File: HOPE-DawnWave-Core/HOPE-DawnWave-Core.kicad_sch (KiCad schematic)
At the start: 40 parts, among them J1 USB_C_Receptacle_USB2.0_16P, SW1 RST, SW2 BOOT, U1 TLV62569DRL, U2 USBLC6-2P6, U3 ESP32-C6-WROOM-1

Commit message: positions of some components - buck converter and usb c - completed
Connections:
- net D+: now also U2.6 (I/O1); no longer U2.4 (I/O2)
- net D-: now also U2.4 (I/O2); no longer U2.6 (I/O1)
- net USB_D+: now also U2.1 (I/O1); no longer U2.3 (I/O2)
- net USB_D-: now also U2.3 (I/O2); no longer U2.1 (I/O1)
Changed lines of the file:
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@@
 		)
 	)
-	(label "D-"
+	(label "D+"
 		(at 81.28 55.88 180)
 		(fields_autoplaced yes)
@@
 		)
 	)
-	(label "USB_D-"
+	(label "USB_D+"
 		(at 57.15 55.88 0)
 		(fields_autoplaced yes)
@@
 		)
 	)
-	(label "D+"
+	(label "D-"
 		(at 81.28 58.42 180)
 		(fields_autoplaced yes)
@@
 		)
 	)
-	(label "USB_D+"
+	(label "USB_D-"
 		(at 57.15 58.42 0)
 		(fields_autoplaced yes)

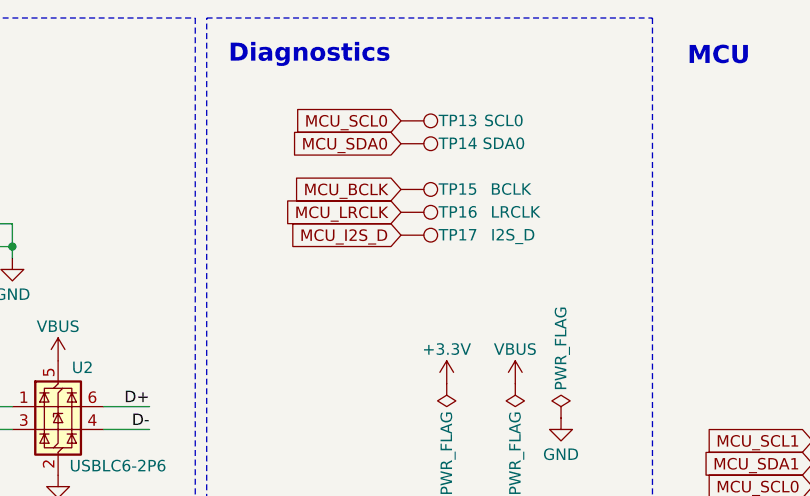
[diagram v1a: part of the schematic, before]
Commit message: flipped esp32 to keep 3.3v on right and 5v on left
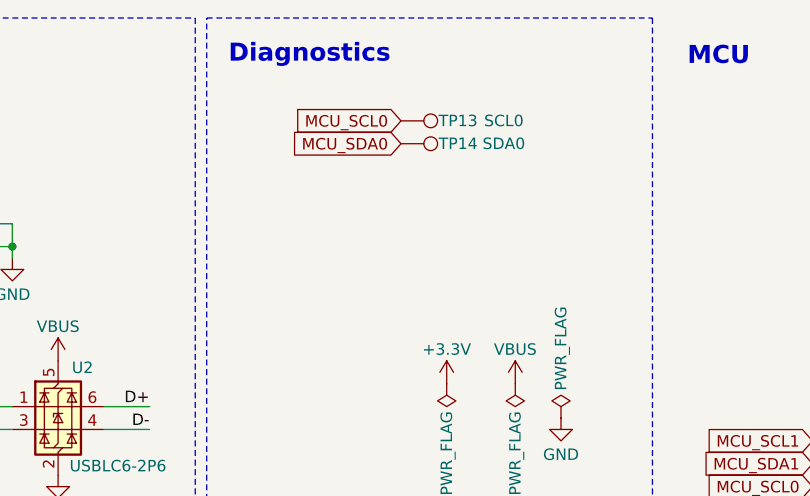
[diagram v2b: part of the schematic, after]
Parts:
- removed TP15: BCLK, TestPoint:TestPoint_Pad_D1.5mm, symbol Connector:TestPoint
- removed TP16: LRCLK, TestPoint:TestPoint_Pad_D1.5mm, symbol Connector:TestPoint
- removed TP17: I2S_D, TestPoint:TestPoint_Pad_D1.5mm, symbol Connector:TestPoint
- TP13, TP14: footprint TestPoint:TestPoint_Pad_D1.5mm -> TestPoint:TestPoint_Pad_D1.0mm

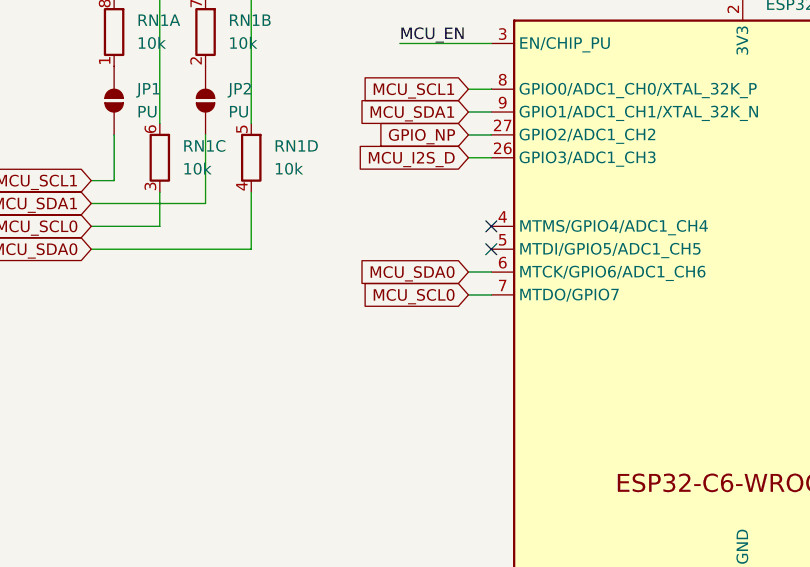
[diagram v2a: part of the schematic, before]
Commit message: fixed gitignore and completed major component placement iteration
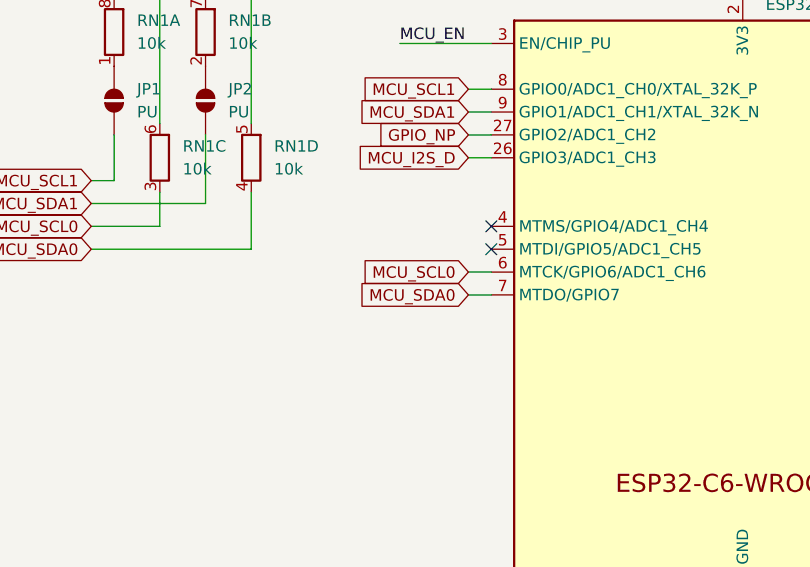
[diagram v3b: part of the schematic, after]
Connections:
- net MCU_SCL0: now also U3.6 (MTCK/GPIO6/ADC1_CH6); no longer U3.7 (MTDO/GPIO7)
- net MCU_SDA0: now also U3.7 (MTDO/GPIO7); no longer U3.6 (MTCK/GPIO6/ADC1_CH6)

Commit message: big progress oops
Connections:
- net GPIO_NP: now also U3.19 (GPIO21); no longer U3.27 (GPIO2/ADC1_CH2)
- net MCU_BACKLIGHT: now also U3.12 (GPIO11); no longer U3.23 (GPIO15)
- net MCU_BCLK: now also U3.17 (GPIO19); no longer U3.25 (U0TXD/GPIO16)
- net MCU_DRST: now also U3.23 (GPIO15); no longer U3.11 (GPIO10)
- net MCU_D/C: now also U3.27 (GPIO2/ADC1_CH2); no longer U3.19 (GPIO21)
- net MCU_I2S_D: now also U3.18 (GPIO20); no longer U3.26 (GPIO3/ADC1_CH3)
- net MCU_LRCLK: now also U3.16 (GPIO18); no longer U3.24 (U0RXD/GPIO17)
- net MCU_MISO: now also U3.24 (U0RXD/GPIO17); no longer U3.16 (GPIO18)
- net MCU_MOSI: now also U3.26 (GPIO3/ADC1_CH3); no longer U3.18 (GPIO20)
- net MCU_SCL0: now also U3.7 (MTDO/GPIO7); no longer U3.6 (MTCK/GPIO6/ADC1_CH6)
- net MCU_SCLK: now also U3.25 (U0TXD/GPIO16); no longer U3.17 (GPIO19)
- net MCU_SDA0: now also U3.6 (MTCK/GPIO6/ADC1_CH6); no longer U3.7 (MTDO/GPIO7)
- net MCU_TD: now also U3.11 (GPIO10); no longer U3.12 (GPIO11)

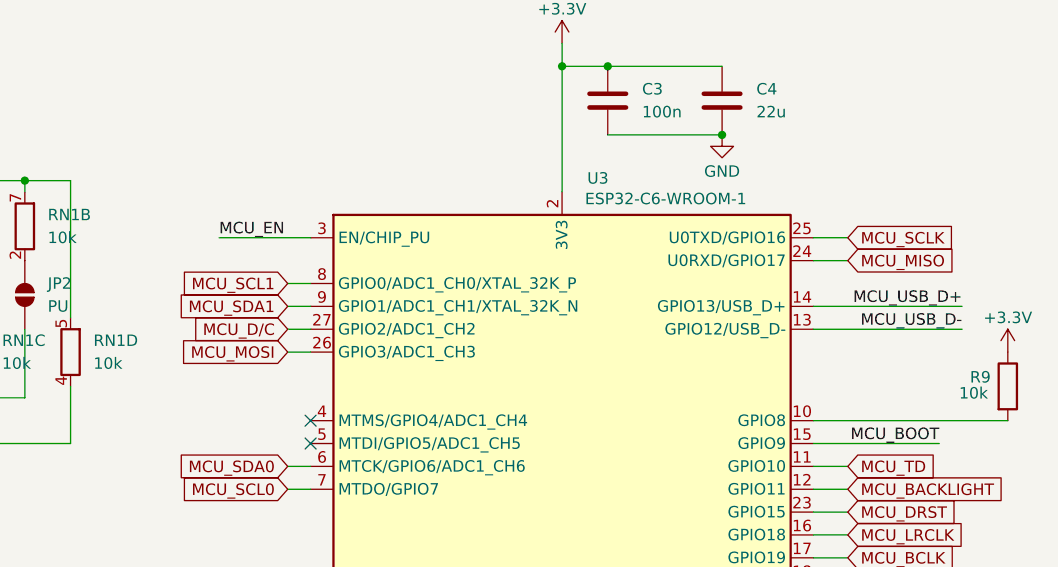
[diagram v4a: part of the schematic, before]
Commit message: Initial layout, need to resolve errors
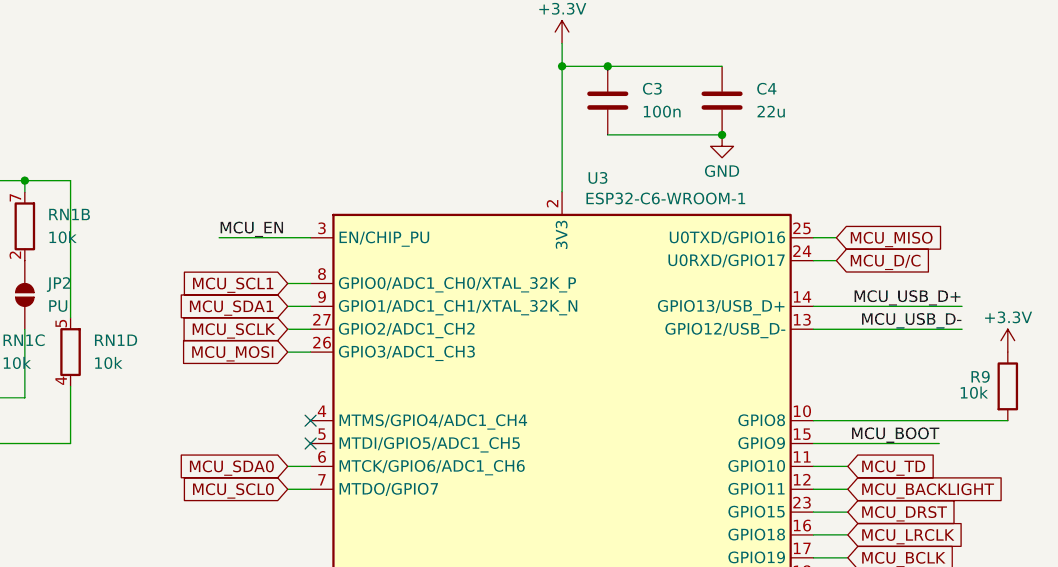
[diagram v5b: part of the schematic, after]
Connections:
- net MCU_D/C: now also U3.24 (U0RXD/GPIO17); no longer U3.27 (GPIO2/ADC1_CH2)
- net MCU_MISO: now also U3.25 (U0TXD/GPIO16); no longer U3.24 (U0RXD/GPIO17)
- net MCU_SCLK: now also U3.27 (GPIO2/ADC1_CH2); no longer U3.25 (U0TXD/GPIO16)

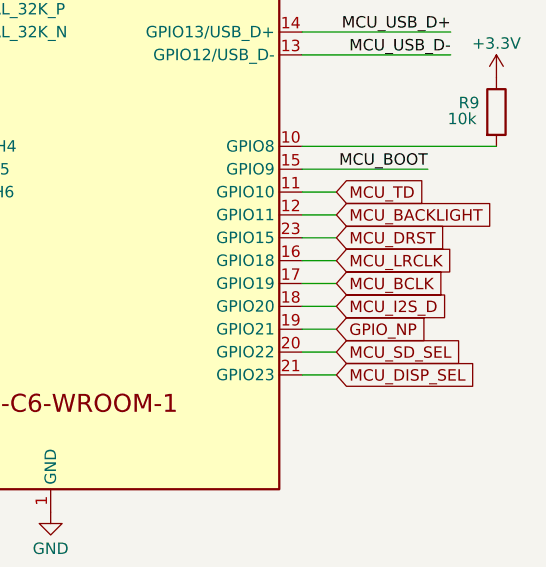
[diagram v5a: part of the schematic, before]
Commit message: fixed spacing on high speed lines, added ground via stitching, made power polygons a bit cleaner, silkscreen labeling is still not done but all warnings are gone
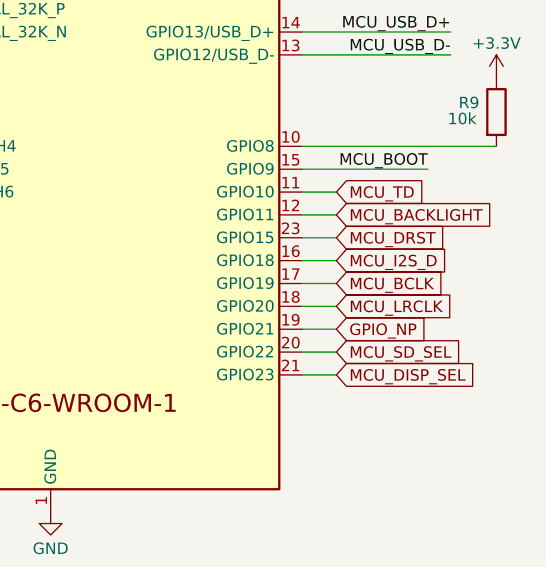
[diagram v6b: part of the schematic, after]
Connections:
- net MCU_I2S_D: now also U3.16 (GPIO18); no longer U3.18 (GPIO20)
- net MCU_LRCLK: now also U3.18 (GPIO20); no longer U3.16 (GPIO18)

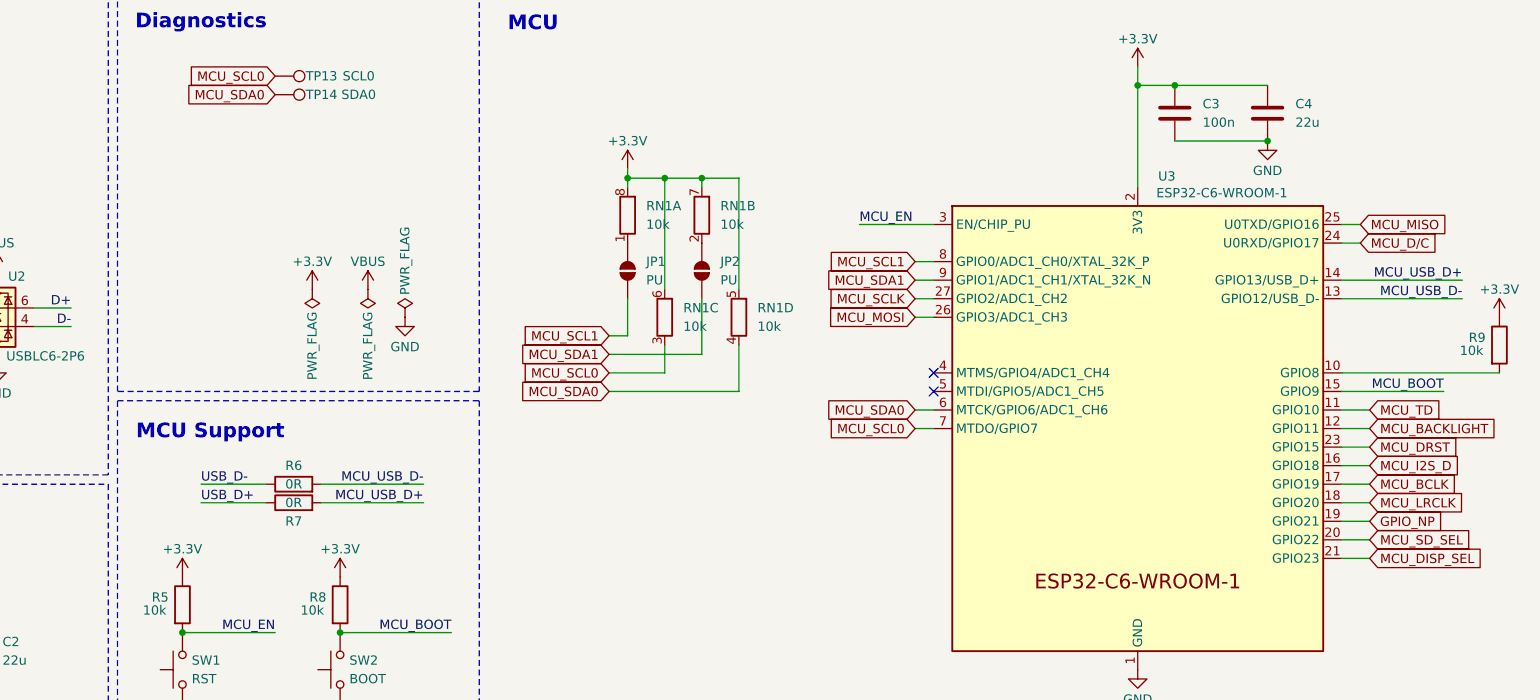
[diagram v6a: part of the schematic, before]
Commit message: corrected eyespi connector wiring and added a 2.54mm pitch header to break it out in case something bad happens
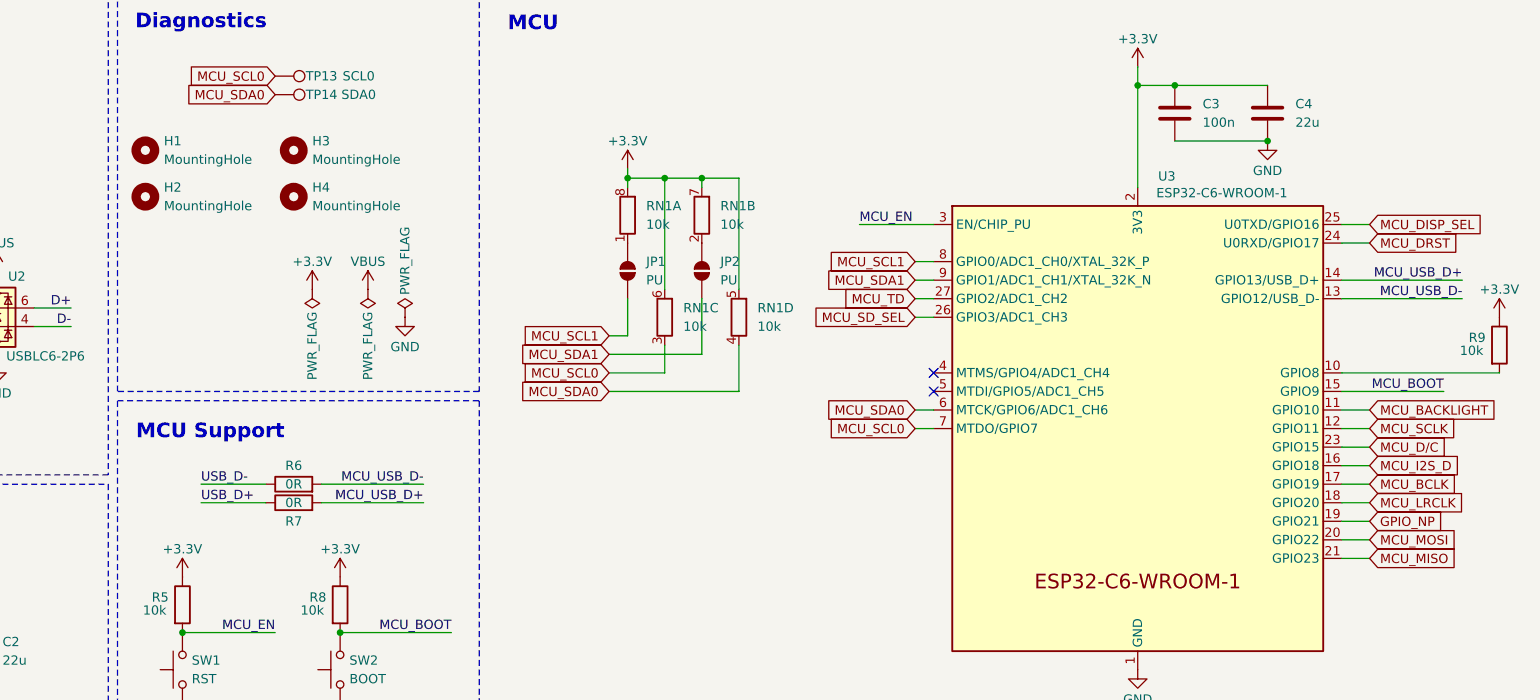
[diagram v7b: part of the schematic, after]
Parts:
- added H1, H2, H3, H4: MountingHole, MountingHole:MountingHole_3.2mm_M3_ISO7380_Pad, symbol Mechanical:MountingHole
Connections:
- net MCU_BACKLIGHT: now also U3.11 (GPIO10); no longer U3.12 (GPIO11)
- net MCU_DISP_SEL: now also U3.25 (U0TXD/GPIO16); no longer U3.21 (GPIO23)
- net MCU_DRST: now also U3.24 (U0RXD/GPIO17); no longer U3.23 (GPIO15)
- net MCU_D/C: now also U3.23 (GPIO15); no longer U3.24 (U0RXD/GPIO17)
- net MCU_MISO: now also U3.21 (GPIO23); no longer U3.25 (U0TXD/GPIO16)
- net MCU_MOSI: now also U3.20 (GPIO22); no longer U3.26 (GPIO3/ADC1_CH3)
- net MCU_SCLK: now also U3.12 (GPIO11); no longer U3.27 (GPIO2/ADC1_CH2)
- net MCU_SD_SEL: now also U3.26 (GPIO3/ADC1_CH3); no longer U3.20 (GPIO22)
- net MCU_TD: now also U3.27 (GPIO2/ADC1_CH2); no longer U3.11 (GPIO10)

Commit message: fab files generated, pcb finalized
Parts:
- R6, R7: value 0R -> 27R
- RN1: value 10k -> 4.7k
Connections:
- net D+: now also U2.4 (I/O2); no longer U2.6 (I/O1)
- net D-: now also U2.6 (I/O1); no longer U2.4 (I/O2)
- net USB_D+: now also U2.3 (I/O2); no longer U2.1 (I/O1)
- net USB_D-: now also U2.1 (I/O1); no longer U2.3 (I/O2)
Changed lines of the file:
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@@
 	(wire
 		(pts
-			(xy 196.85 72.39) (xy 199.39 72.39)
-		)
-		(stroke
-			(width 0)
-			(type default)
-		)
-	)
-	(wire
-		(pts
 			(xy 26.67 68.58) (xy 34.29 68.58)
 		)
@@
 	(wire
 		(pts
+			(xy 196.85 72.39) (xy 199.39 72.39)
+		)
+		(stroke
+			(width 0)
+			(type default)
+		)
+	)
+	(wire
+		(pts
 			(xy 64.77 96.52) (xy 68.58 96.52)
 		)
@@
 	(wire
 		(pts
-			(xy 255.27 72.39) (xy 259.08 72.39)
+			(xy 196.85 69.85) (xy 199.39 69.85)
 		)
 		(stroke
@@
 	(wire
 		(pts
-			(xy 255.27 64.77) (xy 276.86 64.77)
+			(xy 255.27 72.39) (xy 259.08 72.39)
 		)
 		(stroke
@@
 	(wire
 		(pts
-			(xy 55.88 104.14) (xy 49.53 104.14)
+			(xy 255.27 64.77) (xy 276.86 64.77)
 		)
 		(stroke
@@
 	(wire
 		(pts
-			(xy 172.72 38.1) (xy 172.72 53.34)
+			(xy 55.88 104.14) (xy 49.53 104.14)
 		)
 		(stroke
@@
 	(wire
 		(pts
-			(xy 66.04 35.56) (xy 66.04 38.1)
+			(xy 172.72 38.1) (xy 172.72 53.34)
 		)
 		(stroke
@@
 	(wire
 		(pts
-			(xy 196.85 49.53) (xy 199.39 49.53)
+			(xy 66.04 35.56) (xy 66.04 38.1)
 		)
 		(stroke
@@
 	(wire
 		(pts
-			(xy 182.88 138.43) (xy 185.42 138.43)
+			(xy 196.85 49.53) (xy 199.39 49.53)
 		)
 		(stroke
@@
 	(wire
 		(pts
-			(xy 57.15 35.56) (xy 66.04 35.56)
+			(xy 182.88 138.43) (xy 185.42 138.43)
 		)
 		(stroke
@@
 	(wire
 		(pts
-			(xy 57.15 58.42) (xy 66.04 58.42)
+			(xy 76.2 58.42) (xy 81.28 58.42)
 		)
 		(stroke
@@
 	(wire
 		(pts
-			(xy 76.2 55.88) (xy 81.28 55.88)
+			(xy 57.15 35.56) (xy 66.04 35.56)
 		)
 		(stroke
@@
 	(wire
 		(pts
-			(xy 76.2 58.42) (xy 81.28 58.42)
-		)
-		(stroke
-			(width 0)
-			(type default)
-		)
-	)
-	(wire
-		(pts
-			(xy 196.85 69.85) (xy 199.39 69.85)
+			(xy 76.2 55.88) (xy 81.28 55.88)
 		)
 		(stroke
@@
 	(wire
 		(pts
+			(xy 57.15 58.42) (xy 66.04 58.42)
+		)
+		(stroke
+			(width 0)
+			(type default)
+		)
+	)
+	(wire
+		(pts
 			(xy 196.85 57.15) (xy 199.39 57.15)
 		)
@@
 	)
 	(label "D+"
-		(at 81.28 55.88 180)
+		(at 81.28 58.42 180)
 		(fields_autoplaced yes)
 		(effects
@@
 	)
 	(label "USB_D+"
-		(at 57.15 55.88 0)
+		(at 57.15 58.42 0)
 		(fields_autoplaced yes)
 		(effects
@@
 	)
 	(label "D-"
-		(at 81.28 58.42 180)
+		(at 81.28 55.88 180)
 		(fields_autoplaced yes)
 		(effects
@@
 	)
 	(label "USB_D-"
-		(at 57.15 58.42 0)
+		(at 57.15 55.88 0)
 		(fields_autoplaced yes)
 		(effects
@@
 			)
 		)
-		(property "Value" "10k"
+		(property "Value" "4.7k"
 			(at 170.18 44.4499 0)
 			(effects
@@
 			)
 		)
-		(property "Value" "10k"
+		(property "Value" "4.7k"
 			(at 165.1 58.4199 0)
 			(effects
@@
 			)
 		)
-		(property "Value" "0R"
+		(property "Value" "27R"
 			(at 111.76 80.01 90)
 			(effects
@@
 			)
 		)
-		(property "Value" "10k"
+		(property "Value" "4.7k"
 			(at 175.26 58.4199 0)
 			(effects
@@
 			)
 		)
-		(property "Value" "0R"
+		(property "Value" "27R"
 			(at 111.76 82.55 90)
 			(effects
@@
 			)
 		)
-		(property "Value" "10k"
+		(property "Value" "4.7k"
 			(at 160.02 44.4499 0)
 			(effects
